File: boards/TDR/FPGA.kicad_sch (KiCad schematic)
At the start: 13 parts, among them U1 LFE5UM5G-45-CABGA381

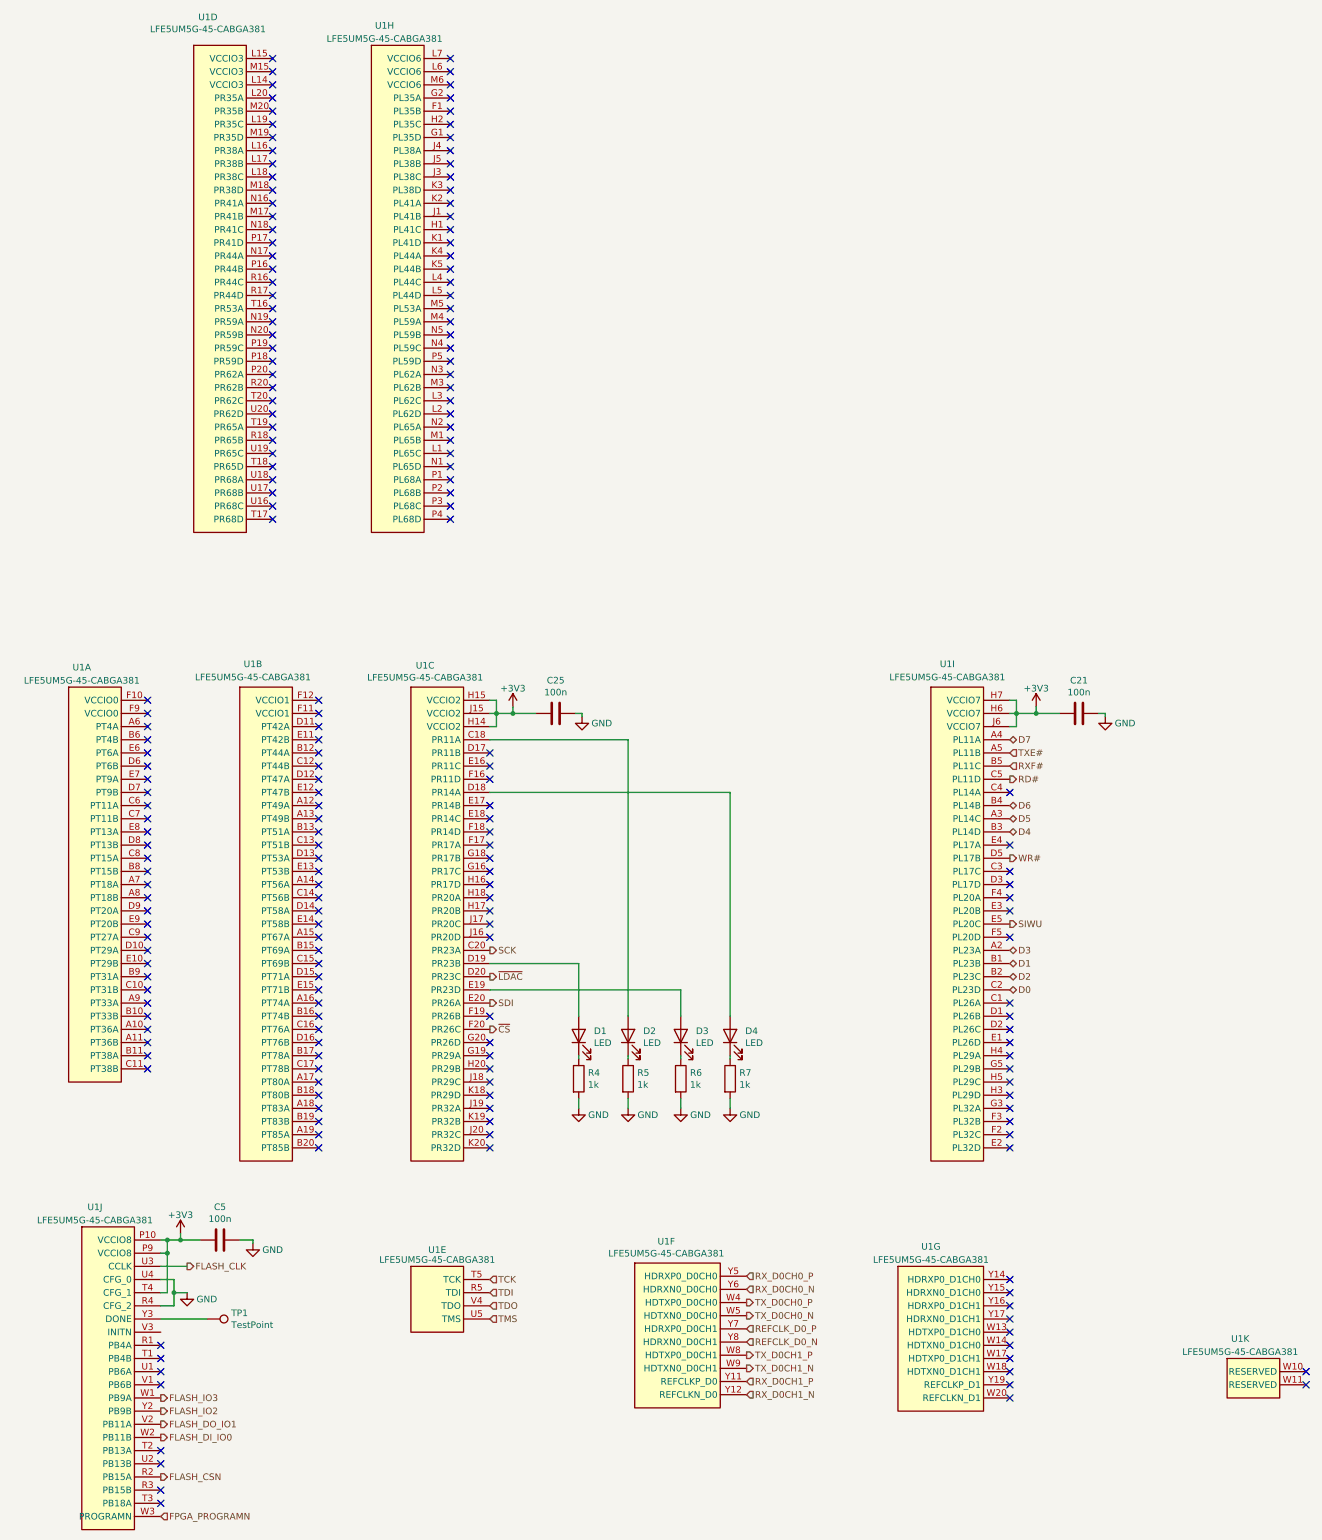
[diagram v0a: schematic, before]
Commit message: Add LD39050PUR feedback resistor values, fixed regulator enable
Fixes #1
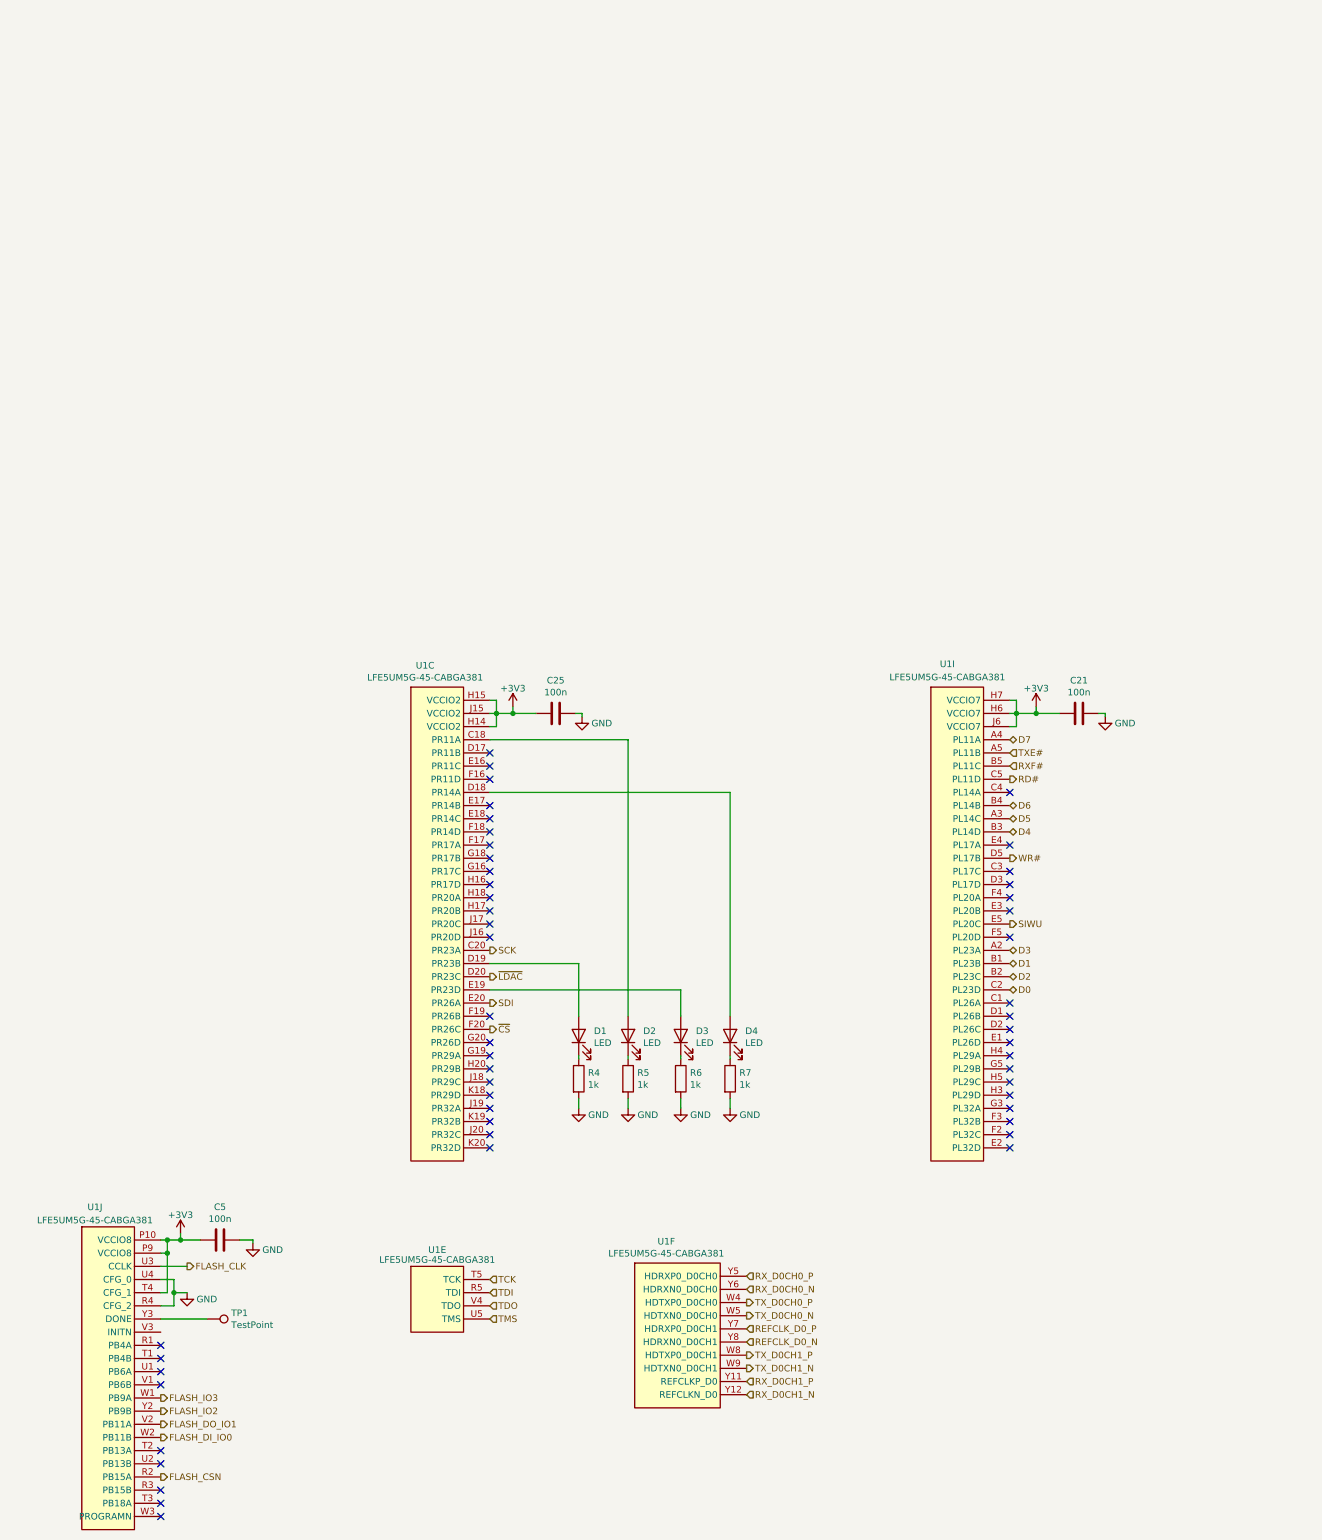
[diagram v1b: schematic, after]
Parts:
- removed unit 11 of U1
- removed unit 7 of U1
- removed unit 1 of U1
- removed unit 2 of U1
- removed unit 4 of U1
- removed unit 8 of U1
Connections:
- net FPGA_PROGRAMN: no longer names the net of U1.W3 (PROGRAMN)
- no-connect marks 199 -> 52
